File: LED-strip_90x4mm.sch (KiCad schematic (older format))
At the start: 18 parts, among them P1 CONN_2, P2 CONN_2, P3 CONN_2, P4 CONN_2, P5 CONN_2, P6 CONN_2

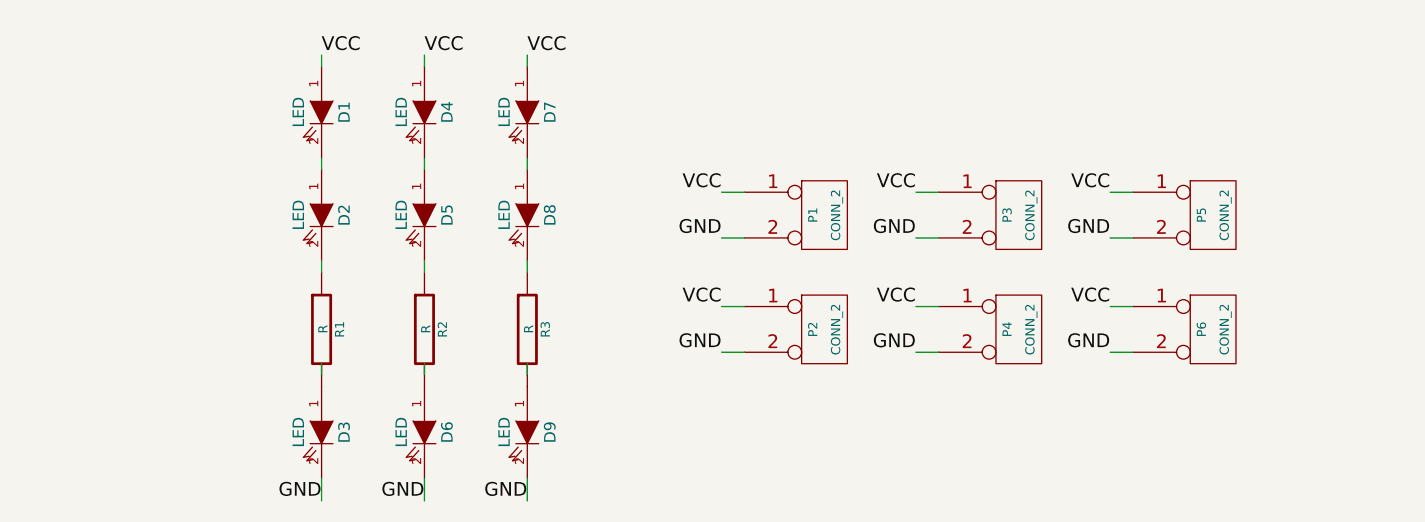
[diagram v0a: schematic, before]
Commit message: Duplicated F_Cu to B_Cu.
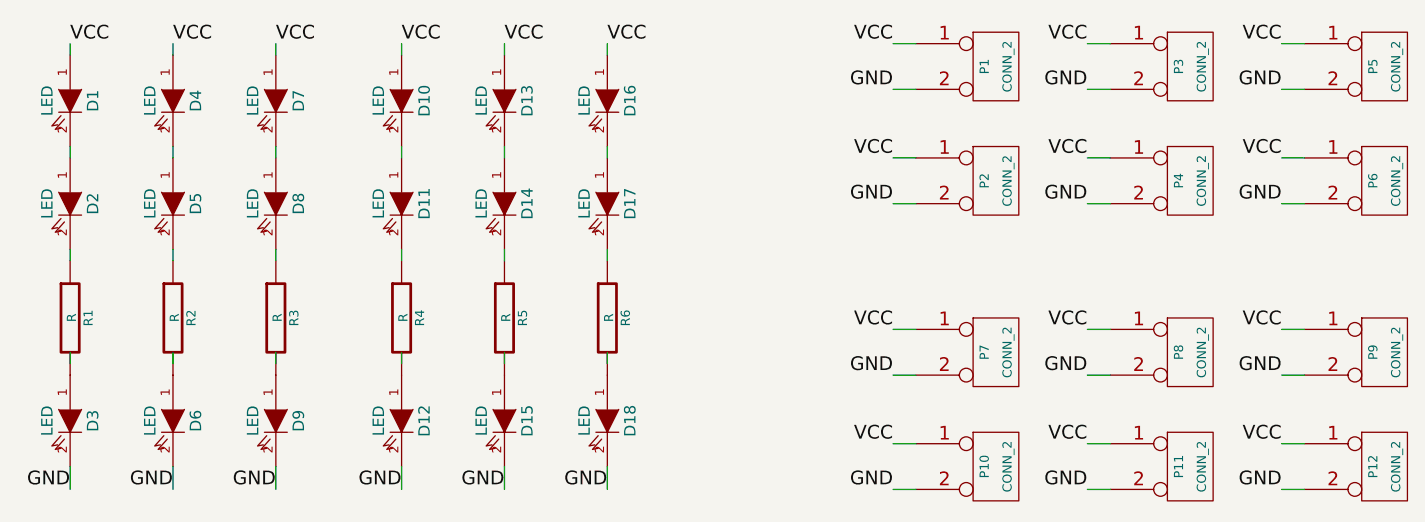
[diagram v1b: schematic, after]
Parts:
- added D10, D11, D12, D13, D14, D15, D16, D17, D18: LED, symbol LED
- added P10, P11, P12, P7, P8, P9: CONN_2, symbol CONN_2
- added R4, R5, R6: R, symbol R
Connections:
- wire segments 27 -> 54
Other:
- moved on the sheet: D1, D2, D3, D4, D5, D6, D7, D8, D9, P1, P2, P3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
